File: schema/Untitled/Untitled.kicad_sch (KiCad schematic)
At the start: 10 parts, among them SW1 SW_Push, SW2 SW_Push, U1 ATtiny84A-P, U2 74HC595, U3 74HC595, U4 CC56-12SURKWA

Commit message: version funcional 1
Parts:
- added R1, R2, R3, R4, R5, R6, R7, R8: R, symbol Device:R
- added TP1, TP2, TP3, TP4: TestPoint_Probe, Connector_Pin:Pin_D1.0mm_L10.0mm, symbol Connector:TestPoint_Probe
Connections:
- net VCC: now reaches U1.1 (VCC)
- net VCC: now also U2.16 (VCC), U3.16 (VCC)
- net s_latch: now reaches U1.10 (PA3)
- net s_latch: now also U2.12 (RCLK), U3.12 (RCLK)
- net GND: now reaches U1.14 (GND)
- net GND: now also U2.13 (~{OE}), U2.8 (GND), U3.13 (~{OE}), U3.8 (GND)
- net s_data: now reaches U1.3 (XTAL2/PB1)
- net s_data: now also U2.14 (SER)
- net reset: now reaches U1.4 (~{RESET}/PB3)
- net reset: now also TP3.1
- net s_clock: now reaches U1.5 (PB2)
- net s_clock: now also U2.11 (SRCLK), U3.11 (SRCLK)
- net s_clear: now reaches U1.6 (PA7)
- net s_clear: now also U2.10 (~{SRCLR}), U3.10 (~{SRCLR})
- net mosi: now reaches U1.7 (PA6)
- net mosi: now also TP2.1
- net miso: now reaches U1.8 (PA5)
- net miso: now also TP1.1
- net sck: now reaches U1.9 (PA4)
- net sck: now also TP4.1
- net at U4.1 (e): now also R5.2
- net at U4.10 (f): now also R6.2
- net at U4.11 (a): now also R1.2
- net at U4.12 (CC1): now also U3.15 (QA)
- net at U4.2 (d): now also R4.2
- net at U4.3 (DPX): now also R8.2
- net at U4.4 (c): now also R3.2
- net at U4.5 (g): now also R7.2
- net at U4.6 (CC4): now also U3.3 (QD)
- net at U4.7 (b): now also R2.2
- net at U4.8 (CC3): now also U3.2 (QC)
- net at U4.9 (CC2): now also U3.1 (QB)
- net at U3.14 (SER): now also U2.9 (QH')
- net at U2.1 (QB): now also R2.1
- net at U2.15 (QA): now also R1.1
- net at U2.2 (QC): now also R3.1
- net at U2.3 (QD): now also R4.1
- net at U2.4 (QE): now also R5.1
- net at U2.5 (QF): now also R6.1
- net at U2.6 (QG): now also R7.1
- net at U2.7 (QH): now also R8.1
- no-connect marks 0 -> 5
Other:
- moved on the sheet: H1, H2, H3, H4, SW1, SW2, U1, U2, U3, U4

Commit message: button prototype
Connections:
- net GND: now also SW1.1
- net at U1.2 (XTAL1/PB0): now also SW1.2
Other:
- moved on the sheet: SW1
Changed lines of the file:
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@@
+	(wire
+		(pts
+			(xy 71.12 95.25) (xy 90.17 95.25)
+		)
+		(stroke
+			(width 0)
+			(type default)
+		)
+	)
 	(wire
 		(pts
@@
 	(wire
 		(pts
+			(xy 90.17 124.46) (xy 78.74 124.46)
+		)
+		(stroke
+			(width 0)
+			(type default)
+		)
+	)
+	(wire
+		(pts
 			(xy 71.12 82.55) (xy 80.01 82.55)
 		)
@@
 		(pts
 			(xy 127 82.55) (xy 134.62 82.55)
+		)
+		(stroke
+			(width 0)
+			(type default)
+		)
+	)
+	(wire
+		(pts
+			(xy 90.17 95.25) (xy 90.17 124.46)
 		)
 		(stroke
@@
 	(symbol
 		(lib_id "Switch:SW_Push")
-		(at 86.36 135.89 0)
+		(at 73.66 124.46 0)
 		(unit 1)
 		(exclude_from_sim no)
@@
 		(fields_autoplaced yes)
 		(property "Reference" "SW1"
-			(at 86.36 128.27 0)
+			(at 73.66 116.84 0)
 			(effects
 				(font
@@
 		)
 		(property "Value" "SW_Push"
-			(at 86.36 130.81 0)
+			(at 73.66 119.38 0)
 			(effects
 				(font
@@
 		)
 		(property "Footprint" ""
-			(at 86.36 130.81 0)
+			(at 73.66 119.38 0)
 			(effects
 				(font
@@
 		)
 		(property "Datasheet" "~"
-			(at 86.36 130.81 0)
+			(at 73.66 119.38 0)
 			(effects
 				(font
@@
 		)
 		(property "Description" "Push button switch, generic, two pins"
-			(at 86.36 135.89 0)
+			(at 73.66 124.46 0)
 			(effects
 				(font
@@
 					(unit 1)
 				)
+			)
+		)
+	)
+	(symbol
+		(lib_id "power:GND")
+		(at 68.58 124.46 0)
+		(unit 1)
+		(exclude_from_sim no)
+		(in_bom yes)
+		(on_board yes)
+		(dnp no)
+		(fields_autoplaced yes)
+		(property "Reference" "#PWR09"
+			(at 68.58 130.81 0)
+			(effects
+				(font
+					(size 1.27 1.27)
+				)
+				(hide yes)
+			)
+		)
+		(property "Value" "GND"
+			(at 68.58 129.54 0)
+			(effects
+				(font
+					(size 1.27 1.27)
+				)
+			)
+		)
+		(property "Footprint" ""
+			(at 68.58 124.46 0)
+			(effects
+				(font
+					(size 1.27 1.27)
+				)
+				(hide yes)
+			)
+		)
+		(property "Datasheet" ""
+			(at 68.58 124.46 0)
+			(effects
+				(font
+					(size 1.27 1.27)
+				)
+				(hide yes)
+			)
+		)
+		(property "Description" "Power symbol creates a global label with name \"GND\" , ground"
+			(at 68.58 124.46 0)
+			(effects
+				(font
+					(size 1.27 1.27)
+				)
+				(hide yes)
+			)
+		)
+		(pin "1"
+		)
+		(instances
+			(project ""
+				(path "/19e0d388-4d21-4b36-b74d-b28bef7280ef"
+					(reference "#PWR09")
+					(unit 1)
+				)

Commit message: surrounding circuits battery, capacitors, probes, etc
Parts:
- added C1: C_Polarized, Capacitor_THT:CP_Radial_D8.0mm_P3.80mm, symbol Device:C_Polarized
- added C2: C, Capacitor_THT:C_Disc_D5.0mm_W2.5mm_P5.00mm, symbol Device:C
- added J1: batteries 2x aa, Connector_Wire:SolderWire-0.1sqmm_1x02_P3.6mm_D0.4mm_OD1mm_Relief, symbol Connector:Conn_01x02_Pin
- added TP5, TP6: TestPoint_Probe, Connector_Pin:Pin_D1.0mm_L10.0mm, symbol Connector:TestPoint_Probe
- R1, R2, R3, R4, R5, R6, R7, R8: footprint (none) -> Resistor_SMD:R_1206_3216Metric_Pad1.30x1.75mm_HandSolder
- SW1, SW2: footprint (none) -> Button_Switch_SMD:SW_Push_1P1T_NO_CK_PTS125Sx43SMTR
- U2, U3: footprint (none) -> Package_DIP:DIP-16_W7.62mm_LongPads
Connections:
- net GND: now also SW2.1, C1.2, C2.2, J1.2 (Pin_2), TP6.1
- net VCC: now also C1.1, C2.1, J1.1 (Pin_1), TP5.1
- net at U1.12 (PA1): now also SW2.2
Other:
- moved on the sheet: SW2

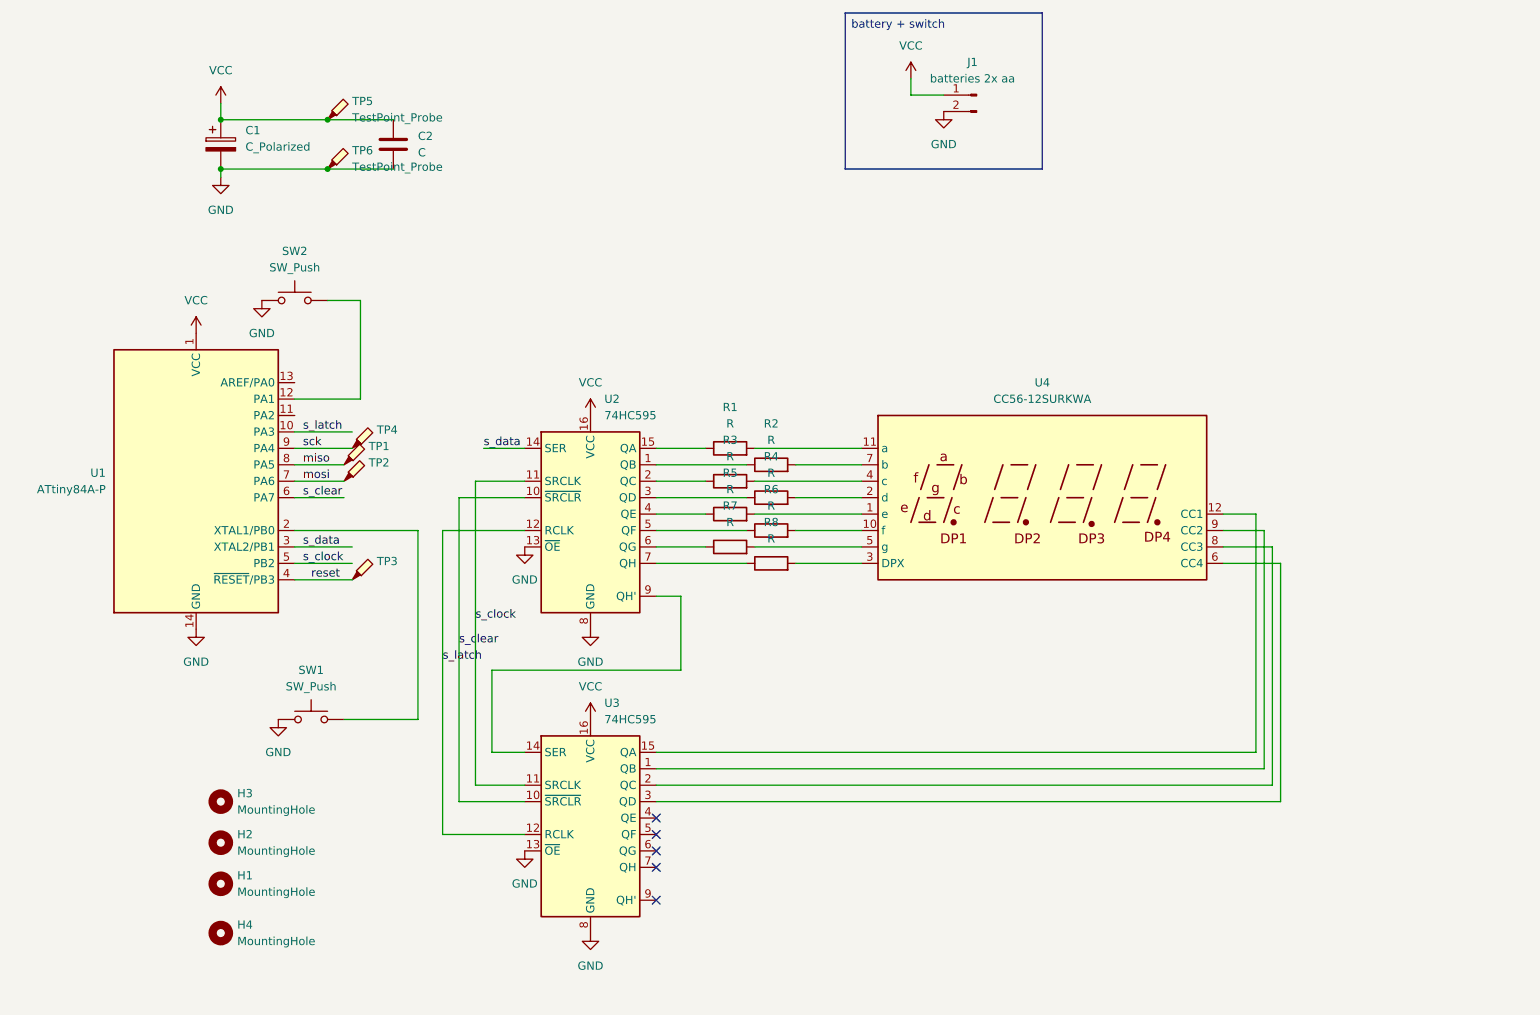
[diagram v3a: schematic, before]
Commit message: pcb with display
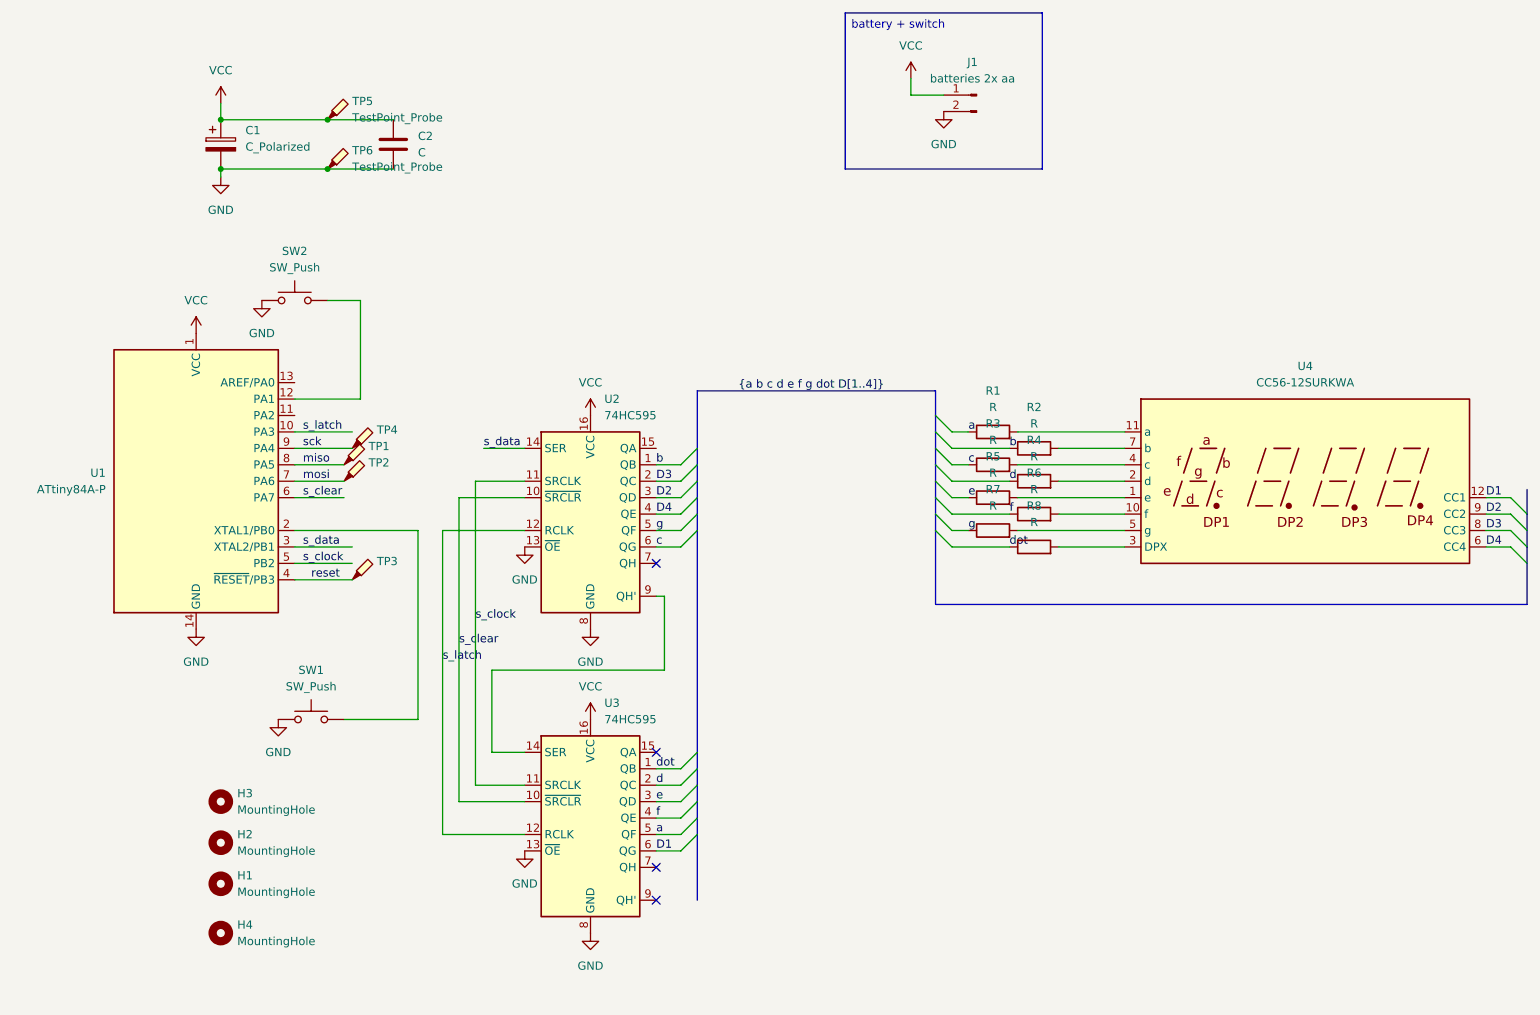
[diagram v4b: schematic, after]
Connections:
- net at U2.15 (QA): no longer R1.1
- net at U3.15 (QA): no longer U4.12 (CC1)
- net D4: now reaches U4.6 (CC4)
- net D4: now also U2.4 (QE); no longer U3.3 (QD)
- net D3: now reaches U4.8 (CC3)
- net D3: now also U2.2 (QC); no longer U3.2 (QC)
- net D2: now reaches U4.9 (CC2)
- net D2: now also U2.3 (QD); no longer U3.1 (QB)
- net c: now reaches U2.6 (QG)
- net c: now also R3.1; no longer R7.1
- net b: now reaches R2.1, U2.1 (QB)
- net d: now reaches R4.1
- net d: now also U3.2 (QC); no longer U2.3 (QD)
- net f: now reaches U3.4 (QE)
- net f: now also R6.1
- net a: now reaches U3.5 (QF)
- net a: now also R1.1
- net D1: now reaches U3.6 (QG)
- net D1: now also U4.12 (CC1)
- net e: now reaches R5.1
- net e: now also U3.3 (QD); no longer U2.4 (QE)
- net at U2.7 (QH): no longer R8.1
- net g: now reaches U2.5 (QF)
- net g: now also R7.1; no longer R6.1
- new net dot: R8.1, U3.1 (QB)
- no-connect marks 5 -> 4
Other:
- moved on the sheet: R1, R2, R3, R4, R5, R6, R7, R8, U4

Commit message: THC
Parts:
- C1: footprint Capacitor_THT:CP_Radial_D8.0mm_P3.80mm -> Capacitor_THT:CP_Radial_D5.0mm_P2.50mm
- SW1, SW2: footprint Button_Switch_SMD:SW_Push_1P1T_NO_CK_PTS125Sx43SMTR -> Button_Switch_SMD:SW_SPST_Omron_B3FS-101xP
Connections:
- net s_clear: now also U1.13 (AREF/PA0); no longer U1.6 (PA7)
- net s_clock: now also U1.12 (PA1); no longer U1.5 (PB2)
- net s_data: now also U1.11 (PA2); no longer U1.3 (XTAL2/PB1)
- net s_latch: now also U1.2 (XTAL1/PB0); no longer U1.10 (PA3)
- net at SW2.2: now also U1.10 (PA3); no longer U1.12 (PA1)
- net at SW1.2: now also U1.6 (PA7); no longer U1.2 (XTAL1/PB0)
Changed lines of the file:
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@@
 	(wire
 		(pts
-			(xy 71.12 90.17) (xy 78.74 90.17)
+			(xy 71.12 72.39) (xy 78.74 72.39)
 		)
 		(stroke
@@
 	(wire
 		(pts
-			(xy 81.28 74.93) (xy 71.12 74.93)
-		)
-		(stroke
-			(width 0)
-			(type default)
-		)
-	)
-	(wire
-		(pts
 			(xy 93.98 95.25) (xy 106.68 95.25)
 		)
@@
 	(wire
 		(pts
-			(xy 71.12 100.33) (xy 80.01 100.33)
+			(xy 71.12 74.93) (xy 80.01 74.93)
 		)
 		(stroke
@@
 	(wire
 		(pts
-			(xy 71.12 97.79) (xy 80.01 97.79)
+			(xy 71.12 77.47) (xy 80.01 77.47)
 		)
 		(stroke
@@
 	(wire
 		(pts
-			(xy 71.12 80.01) (xy 80.01 80.01)
+			(xy 71.12 95.25) (xy 80.01 95.25)
 		)
 		(stroke
@@
 	(wire
 		(pts
+			(xy 81.28 80.01) (xy 71.12 80.01)
+		)
+		(stroke
+			(width 0)
+			(type default)
+		)
+	)
+	(wire
+		(pts
 			(xy 189.23 82.55) (xy 199.39 82.55)
 		)
@@
 		)
 	)
+	(wire
+		(pts
+			(xy 90.17 90.17) (xy 90.17 124.46)
+		)
+		(stroke
+			(width 0)
+			(type default)
+		)
+	)
 	(bus
 		(pts
@@
 	(wire
 		(pts
-			(xy 81.28 59.69) (xy 81.28 74.93)
+			(xy 90.17 90.17) (xy 71.12 90.17)
 		)
 		(stroke
@@
 	(wire
 		(pts
-			(xy 71.12 95.25) (xy 90.17 95.25)
-		)
-		(stroke
-			(width 0)
-			(type default)
-		)
-	)
-	(wire
-		(pts
 			(xy 127 137.16) (xy 130.81 137.16)
 		)
@@
 		)
 	)
+	(wire
+		(pts
+			(xy 81.28 59.69) (xy 81.28 80.01)
+		)
+		(stroke
+			(width 0)
+			(type default)
+		)
+	)
 	(bus
 		(pts
@@
 	(wire
 		(pts
-			(xy 90.17 95.25) (xy 90.17 124.46)
-		)
-		(stroke
-			(width 0)
-			(type default)
-		)
-	)
-	(wire
-		(pts
 			(xy 128.27 116.84) (xy 101.6 116.84)
 		)
@@
 	)
 	(label "s_latch"
-		(at 72.39 80.01 0)
+		(at 72.39 95.25 0)
 		(effects
 			(font
@@
 	)
 	(label "s_clock"
-		(at 72.39 100.33 0)
+		(at 72.39 74.93 0)
 		(effects
 			(font
@@
 	)
 	(label "s_data"
-		(at 72.39 97.79 0)
+		(at 72.39 77.47 0)
 		(effects
 			(font
@@
 	)
 	(label "s_clear"
-		(at 72.39 90.17 0)
+		(at 72.39 72.39 0)
 		(effects
 			(font
@@
 			)
 		)
-		(property "Footprint" "Button_Switch_SMD:SW_Push_1P1T_NO_CK_PTS125Sx43SMTR"
+		(property "Footprint" "Button_Switch_SMD:SW_SPST_Omron_B3FS-101xP"
 			(at 73.66 119.38 0)
 			(effects
@@
 			)
 		)
-		(property "Footprint" "Capacitor_THT:CP_Radial_D8.0mm_P3.80mm"
+		(property "Footprint" "Capacitor_THT:CP_Radial_D5.0mm_P2.50mm"
 			(at 60.6552 39.37 0)
 			(effects
@@
 			)
 		)
-		(property "Footprint" "Button_Switch_SMD:SW_Push_1P1T_NO_CK_PTS125Sx43SMTR"
+		(property "Footprint" "Button_Switch_SMD:SW_SPST_Omron_B3FS-101xP"
 			(at 71.12 54.61 0)
 			(effects

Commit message: ultimos toques a la pcb
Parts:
- U1: footprint Package_DIP:DIP-14_W7.62mm -> Package_DIP:DIP-14_W7.62mm_SMDSocket_SmallPads
- U2, U3: footprint Package_DIP:DIP-16_W7.62mm_LongPads -> Package_DIP:DIP-16_W7.62mm_SMDSocket_SmallPads
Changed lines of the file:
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@@
 			)
 		)
-		(property "Footprint" "Package_DIP:DIP-14_W7.62mm"
+		(property "Footprint" "Package_DIP:DIP-14_W7.62mm_SMDSocket_SmallPads"
 			(at 55.88 87.63 0)
 			(effects
@@
 			)
 		)
-		(property "Footprint" "Package_DIP:DIP-16_W7.62mm_LongPads"
+		(property "Footprint" "Package_DIP:DIP-16_W7.62mm_SMDSocket_SmallPads"
 			(at 116.84 139.7 0)
 			(effects
@@
 			)
 		)
-		(property "Footprint" "Package_DIP:DIP-16_W7.62mm_LongPads"
+		(property "Footprint" "Package_DIP:DIP-16_W7.62mm_SMDSocket_SmallPads"
 			(at 116.84 92.71 0)
 			(effects
